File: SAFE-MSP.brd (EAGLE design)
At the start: 19 x 16.5 mm, 3 parts

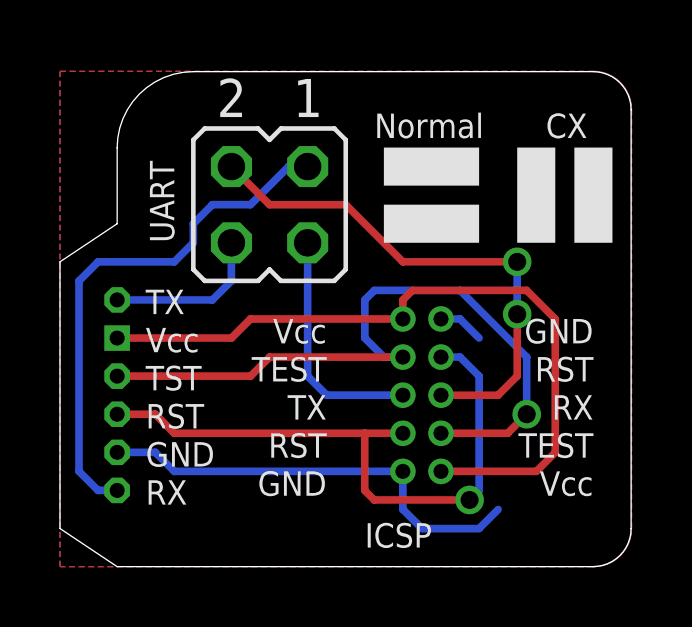
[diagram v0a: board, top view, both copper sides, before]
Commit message: bug fixes
updated iso board to new pinout and rj-12 connector
cleaned up safe-msp board
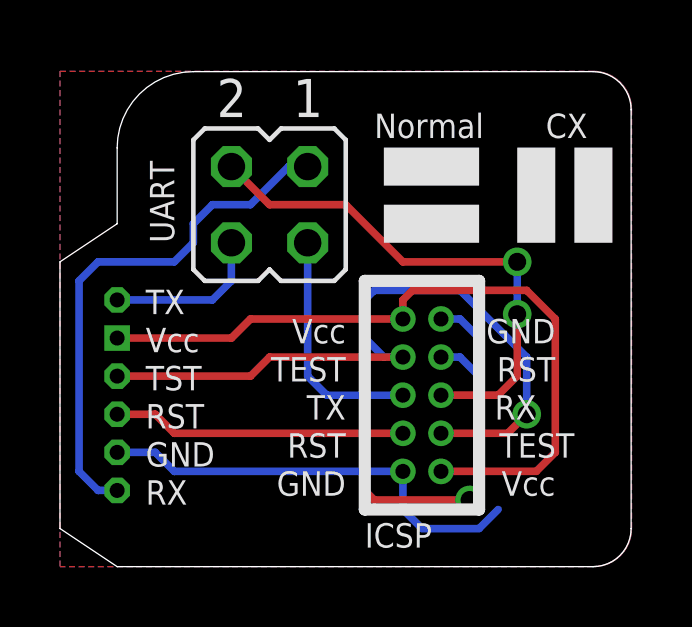
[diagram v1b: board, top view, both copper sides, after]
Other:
- board text added: "GND"
- board text added: "RST"
- board text added: "RX"
- board text added: "TEST"
- board text added: "TX"
- board text added: "Vcc"
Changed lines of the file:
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@@
 <grid distance="0.025" unitdist="inch" unit="inch" style="lines" multiple="1" display="yes" altdistance="0.00625" altunitdist="inch" altunit="inch"/>
 <layers>
-<layer number="1" name="Top" color="4" fill="1" visible="yes" active="yes"/>
+<layer number="1" name="Top" color="4" fill="1" visible="no" active="yes"/>
 <layer number="16" name="Bottom" color="1" fill="1" visible="no" active="yes"/>
 <layer number="17" name="Pads" color="2" fill="1" visible="yes" active="yes"/>
@@
 <layer number="23" name="tOrigins" color="15" fill="1" visible="yes" active="yes"/>
 <layer number="24" name="bOrigins" color="15" fill="1" visible="yes" active="yes"/>
-<layer number="25" name="tNames" color="7" fill="1" visible="yes" active="yes"/>
+<layer number="25" name="tNames" color="7" fill="1" visible="no" active="yes"/>
 <layer number="26" name="bNames" color="7" fill="1" visible="yes" active="yes"/>
 <layer number="27" name="tValues" color="7" fill="1" visible="yes" active="yes"/>
@@
 <text x="16.1925" y="14.2875" size="0.8128" layer="121">CX</text>
 <text x="3.81" y="10.795" size="0.8128" layer="121" rot="R90">UART</text>
+<text x="3.33375" y="8.5725" size="0.8128" layer="122" rot="MR180">Vcc</text>
+<text x="3.4925" y="3.4925" size="0.8128" layer="122" rot="MR180">GND</text>
+<text x="3.4925" y="4.7625" size="0.8128" layer="122" rot="MR180">RST</text>
+<text x="2.69875" y="7.3025" size="0.8128" layer="122" rot="MR180">TEST</text>
+<text x="4.1275" y="6.0325" size="0.8128" layer="122" rot="MR180">TX</text>
+<text x="6.6675" y="3.4925" size="0.8128" layer="122" rot="MR180">Vcc</text>
+<text x="6.6675" y="8.5725" size="0.8128" layer="122" rot="MR180">GND</text>
+<text x="6.6675" y="7.3025" size="0.8128" layer="122" rot="MR180">RST</text>
+<text x="6.6675" y="4.7625" size="0.8128" layer="122" rot="MR180">TEST</text>
+<text x="6.6675" y="6.0325" size="0.8128" layer="122" rot="MR180">RX</text>
 </plain>
 <attributes>
@@
 <elements>
 <element name="U$1" library="LaunchFET" package="SAFEMSP" value="6-PIN-ICSPSAFE-MSP" x="11.43" y="3.175" smashed="yes"/>
-<element name="U$2" library="LaunchFET" package="EASYMSP-6PIN" value="6-PIN-ICSPEASY-MSP" x="1.905" y="5.08"/>
+<element name="U$2" library="LaunchFET" package="EASYMSP-6PIN" value="6-PIN-ICSPEASY-MSP" x="1.905" y="5.08" smashed="yes"/>
 <element name="JP1" library="jumper" package="JP2Q" value="" x="6.985" y="12.065" smashed="yes" rot="R180">
 <attribute name="VALUE" x="2.54" y="14.605" size="1.27" layer="27" ratio="10" rot="R270"/>
